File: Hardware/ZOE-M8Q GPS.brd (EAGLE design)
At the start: 25.4 x 25.4 mm, 60 parts, among them J4 U.FL, U1 UBLOX_ZOE_M8-0-10, Y1 32.768kHz

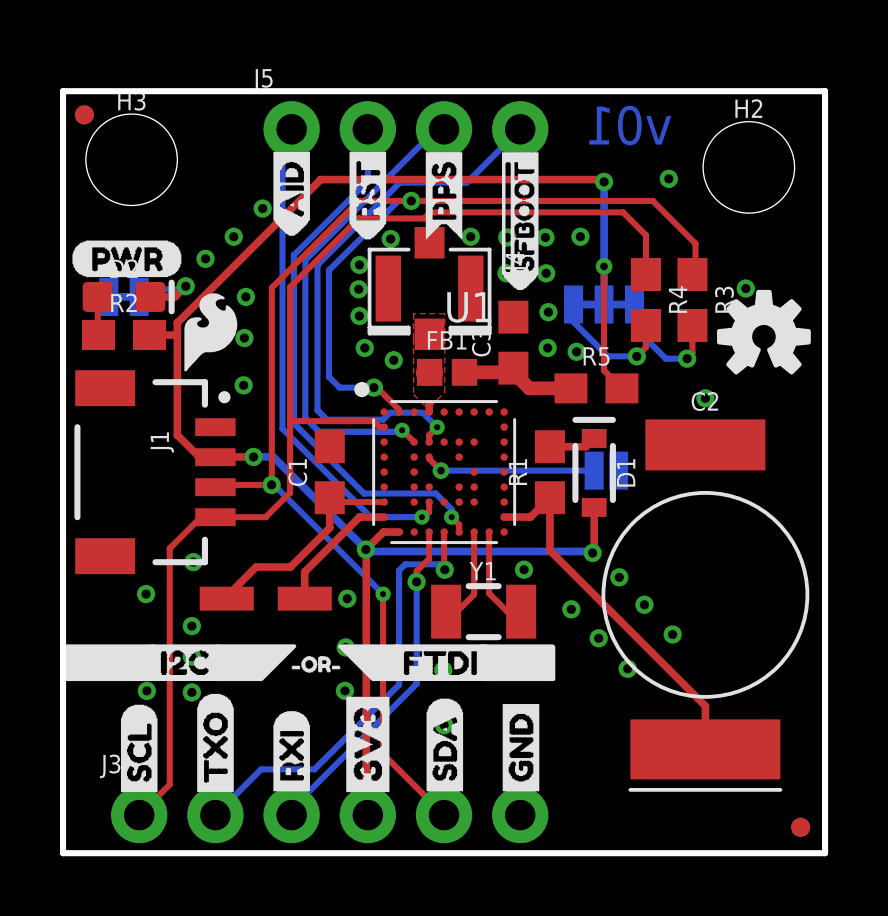
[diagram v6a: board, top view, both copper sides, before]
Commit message: Adds traces for unconnected ground pins, and changes 1k resistor to 100
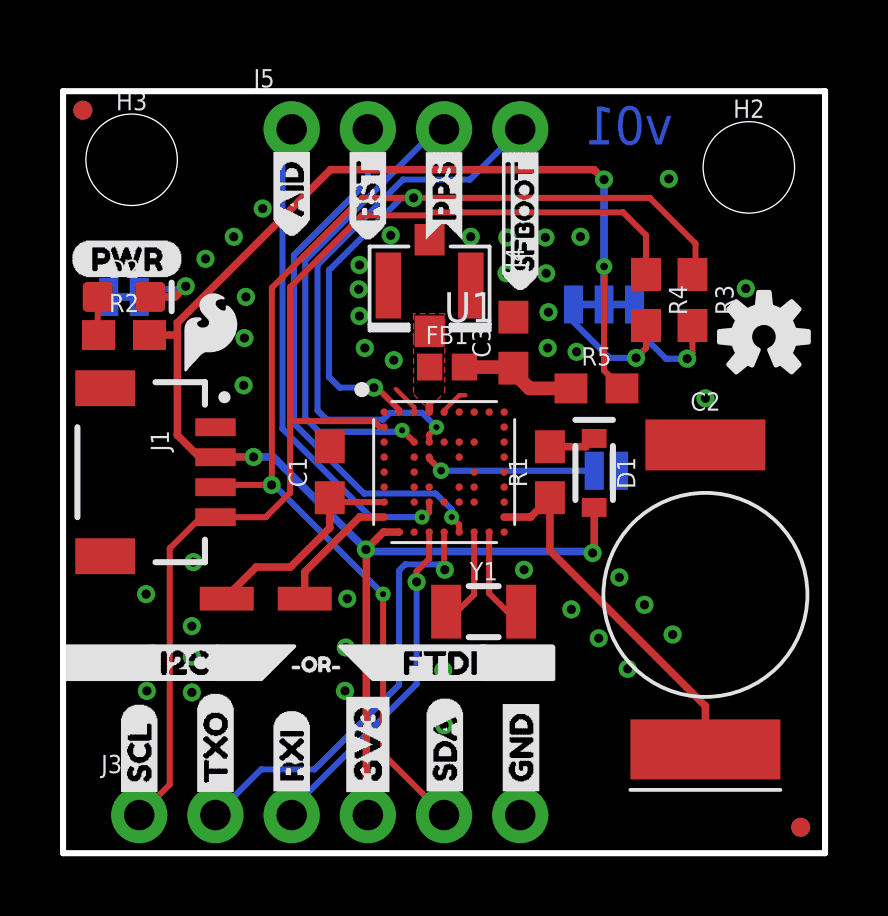
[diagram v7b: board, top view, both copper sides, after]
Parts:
- R1: value 1k -> 100
- moved FB1 0.18 mm to (12.8, 16.2)
- moved FD1 0.16 mm to (0.66, 24.8)
- moved FD3 0.16 mm to (0.66, 24.8)
- moved J4 0.10 mm to (12.2, 18.9)
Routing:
- net GND: track 0.00 -> 2.01 mm

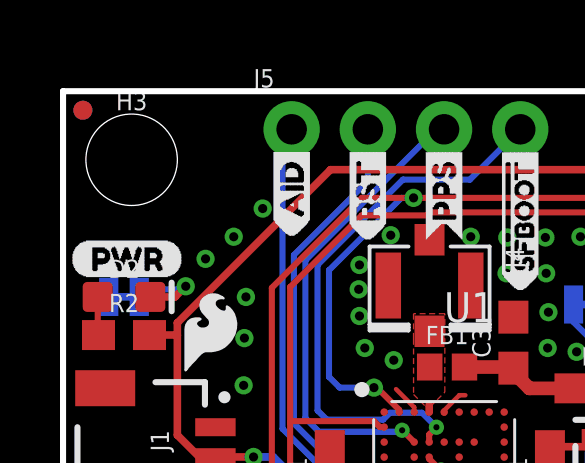
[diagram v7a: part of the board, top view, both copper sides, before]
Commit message: Moves left standoff to be symmetrical with right, and adds measurements to standoffs
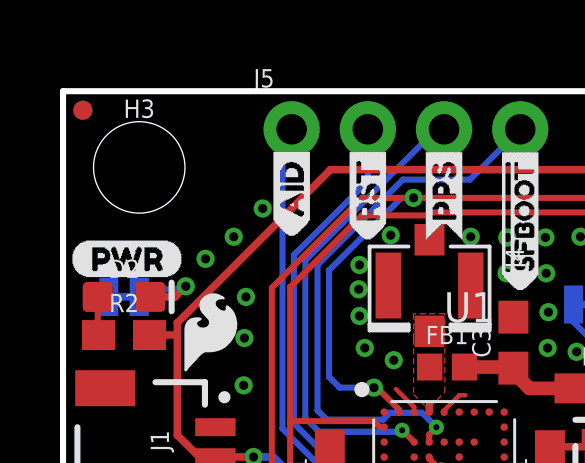
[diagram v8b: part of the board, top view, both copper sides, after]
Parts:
- moved H3 0.36 mm to (2.54, 22.9)
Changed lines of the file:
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@@
 <drawing>
 <settings>
-<setting alwaysvectorfont="yes"/>
+<setting alwaysvectorfont="no"/>
 <setting verticaltext="up"/>
 </settings>
-<grid distance="0.05" unitdist="inch" unit="inch" style="lines" multiple="1" display="yes" altdistance="0.001" altunitdist="inch" altunit="inch"/>
+<grid distance="0.05" unitdist="inch" unit="inch" style="lines" multiple="1" display="yes" altdistance="0.005" altunitdist="inch" altunit="inch"/>
 <layers>
 <layer number="1" name="Top" color="4" fill="1" visible="yes" active="yes"/>
@@
 <layer number="39" name="tKeepout" color="4" fill="11" visible="yes" active="yes"/>
 <layer number="40" name="bKeepout" color="1" fill="11" visible="no" active="yes"/>
-<layer number="41" name="tRestrict" color="4" fill="10" visible="yes" active="yes"/>
+<layer number="41" name="tRestrict" color="4" fill="10" visible="no" active="yes"/>
 <layer number="42" name="bRestrict" color="1" fill="10" visible="no" active="yes"/>
 <layer number="43" name="vRestrict" color="2" fill="10" visible="no" active="yes"/>
@@
 <layer number="45" name="Holes" color="7" fill="1" visible="yes" active="yes"/>
 <layer number="46" name="Milling" color="3" fill="1" visible="no" active="yes"/>
-<layer number="47" name="Measures" color="7" fill="1" visible="no" active="yes"/>
+<layer number="47" name="Measures" color="7" fill="1" visible="yes" active="yes"/>
 <layer number="48" name="Document" color="7" fill="1" visible="no" active="yes"/>
 <layer number="49" name="Reference" color="13" fill="1" visible="yes" active="yes"/>
@@
 <layer number="115" name="ReferenceISLANDS" color="7" fill="1" visible="no" active="no"/>
 <layer number="116" name="Patch_BOT" color="9" fill="4" visible="no" active="no"/>
-<layer number="117" name="PM_Ref" color="26" fill="1" visible="no" active="yes"/>
+<layer number="117" name="PM_Ref" color="26" fill="1" visible="yes" active="yes"/>
 <layer number="118" name="Rect_Pads" color="7" fill="1" visible="no" active="no"/>
-<layer number="119" name="PF_Ref" color="31" fill="1" visible="no" active="yes"/>
-<layer number="120" name="WFL_Ref" color="25" fill="1" visible="no" active="yes"/>
+<layer number="119" name="PF_Ref" color="31" fill="1" visible="yes" active="yes"/>
+<layer number="120" name="WFL_Ref" color="25" fill="1" visible="yes" active="yes"/>
 <layer number="121" name="_tsilk" color="7" fill="1" visible="no" active="no"/>
 <layer number="122" name="_bsilk" color="7" fill="1" visible="no" active="no"/>
@@
 </polygon>
 <dimension x1="0" y1="25.4" x2="25.4" y2="25.4" x3="12.7" y3="31.75" textsize="1.27" textratio="15" layer="47" dtype="vertical" unit="inch"/>
-<text x="6.35" y="29.21" size="1.27" layer="47" font="vector" ratio="15">Units in Inches</text>
+<text x="8.89" y="26.67" size="1.27" layer="47" font="vector" ratio="15">Units in Inches</text>
 <wire x1="15.875" y1="7.0612" x2="12.1666" y2="7.0612" width="0.127" layer="41"/>
 <wire x1="12.1666" y1="7.0612" x2="12.1666" y2="9.0424" width="0.127" layer="41"/>
@@
 <wire x1="14.3764" y1="9.0424" x2="15.875" y2="9.0424" width="0.127" layer="41"/>
 <wire x1="15.875" y1="9.0424" x2="15.875" y2="7.0612" width="0.127" layer="41"/>
+<dimension x1="2.54" y1="22.86" x2="0" y2="22.86" x3="1.27" y3="29.21" textsize="1.27" textratio="15" layer="47" unit="inch"/>
+<dimension x1="22.86" y1="22.86" x2="22.86" y2="25.4" x3="29.21" y3="24.13" textsize="1.27" textratio="15" layer="47" unit="inch"/>
 </plain>
 <attributes>
@@
 <attribute name="VALUE" x="22.86" y="21.209" size="0.6096" layer="27" font="vector" ratio="20" align="top-center"/>
 </element>
-<element name="H3" library="SparkFun-Hardware" package="STAND-OFF-TIGHT" value="STAND-OFFTIGHT" x="2.286" y="23.114" smashed="yes">
-<attribute name="NAME" x="2.286" y="24.765" size="0.6096" layer="25" font="vector" ratio="20" align="bottom-center"/>
-<attribute name="VALUE" x="2.286" y="21.463" size="0.6096" layer="27" font="vector" ratio="20" align="top-center"/>
+<element name="H3" library="SparkFun-Hardware" package="STAND-OFF-TIGHT" value="STAND-OFFTIGHT" x="2.54" y="22.86" smashed="yes">
+<attribute name="NAME" x="2.54" y="24.511" size="0.6096" layer="25" font="vector" ratio="20" align="bottom-center"/>
+<attribute name="VALUE" x="2.54" y="21.209" size="0.6096" layer="27" font="vector" ratio="20" align="top-center"/>
 </element>
 <element name="JP1" library="SparkFun-Jumpers" package="SMT-JUMPER_2_NO_SILK" value="JUMPER-SMT_2_NO_SILK" x="18.1102" y="12.7508" smashed="yes" rot="MR180">
